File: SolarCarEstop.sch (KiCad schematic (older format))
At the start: 49 parts

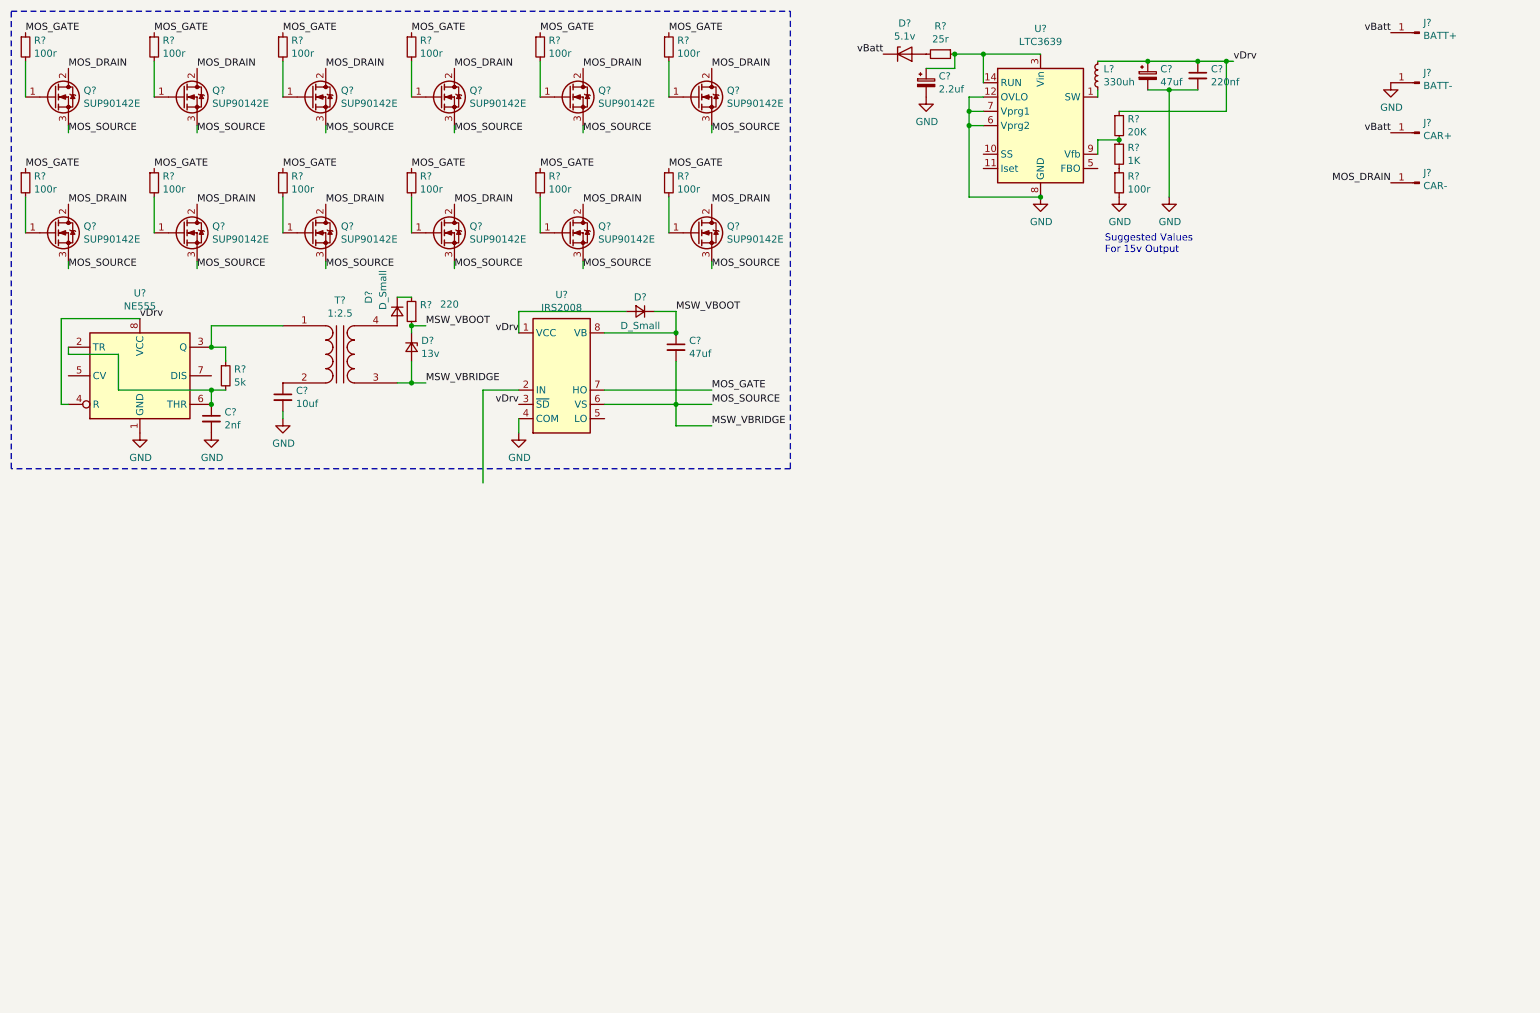
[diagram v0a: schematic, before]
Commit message: Add emergency button, BMS fault output, and BMS fault input
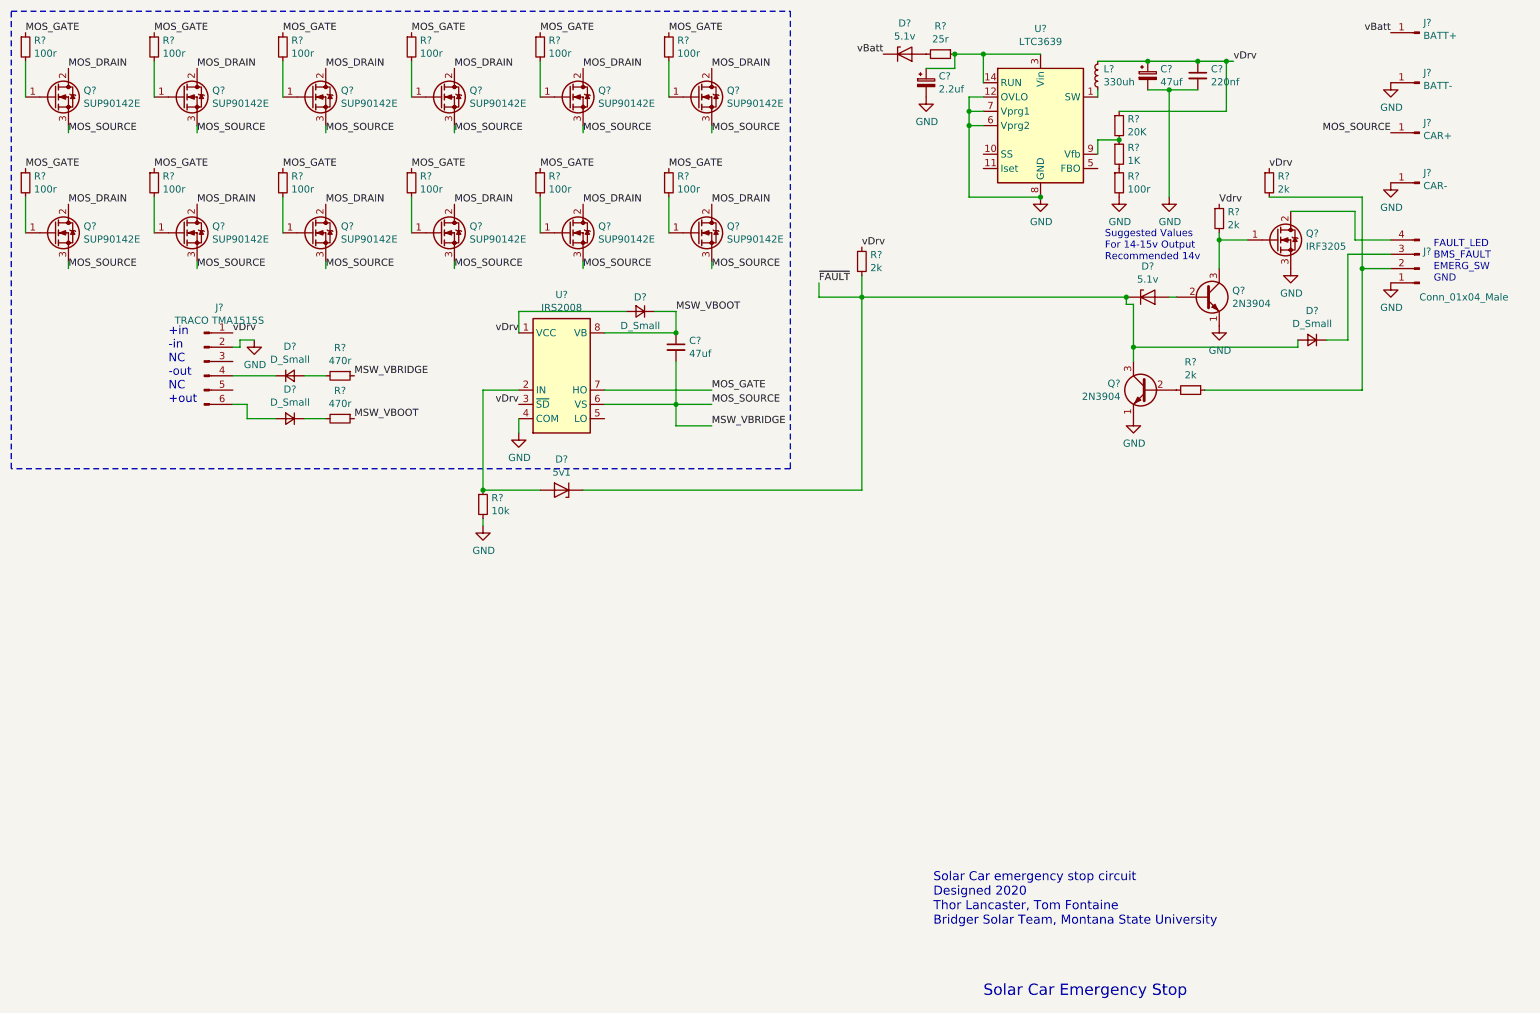
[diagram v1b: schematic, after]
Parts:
- removed C?: 10uf, symbol Device:C_Small
- removed C?: 2nf, symbol Device:C_Small
- removed D?: D_Small, symbol Device:D_Small
- removed D?: 13v, symbol Device:D_Zener_Small
- removed R?: 220, symbol Device:R_Small
- removed R?: 5k, symbol Device:R_Small
- removed T?: 1:2.5, symbol Device:Transformer_1P_1S
- removed U?: NE555, symbol Timer:NE555
- added D? (x3): D_Small, symbol Device:D_Small
- added D?: 5.1v, symbol Device:D_Zener
- added D?: 5v1, symbol Device:D_Zener
- added J?: TRACO TMA1515S, symbol Connector:Conn_01x06_Male
- added J?: Conn_01x04_Male, symbol Connector:Conn_01x04_Male
- added Q?: IRF3205, Package_TO_SOT_THT:TO-220-3_Vertical, symbol Transistor_FET:IRF3205
- added Q? (x2): 2N3904, Package_TO_SOT_THT:TO-92_Inline, symbol Transistor_BJT:2N3904
- added R? (x2): 470r, symbol Device:R_Small
- added R? (x4): 2k, symbol Device:R_Small
- added R?: 10k, symbol Device:R_Small
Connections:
- net GND: now also J?.1 (Pin_1), J?.1 (Pin_1), J?.2 (Pin_2), Q?.1 (E), Q?.1 (E), Q?.3 (S), R?.2
- net MOS_DRAIN: no longer J?.1 (Pin_1)
- net MOS_SOURCE: now also J?.1 (Pin_1), R?.1
- net MSW_VBOOT: now also R?.1
- net vBatt: no longer J?.1 (Pin_1)
- net vDrv: now also J?.1 (Pin_1), R?.1, R?.1
- net at U?.2 (IN): now also D?.2 (A), R?.1
- new net: D?.1 (K), J?.4 (Pin_4)
- new net: D?.2 (A), J?.6 (Pin_6)
- new net: D?.2 (A), R?.2
- new net: D?.1 (K), R?.2
- new net: J?.2 (Pin_2), R?.1, R?.2
- new net: D?.1 (K), J?.3 (Pin_3)
- new net: J?.4 (Pin_4), Q?.2 (D)
- new net: Q?.1 (G), Q?.3 (C), R?.2
- new net: D?.2 (A), Q?.2 (B)
- new net: Q?.2 (B), R?.2
- new net Vdrv: R?.1
- new net ~FAULT: D?.1 (K), D?.1 (K), D?.2 (A), Q?.3 (C), R?.2
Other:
- note added: "+in\n-in\nNC\n-out\nNC\n+out"
- note added: "FAULT_LED\nBMS_FAULT\nEMERG_SW\nGND"
- note added: "Solar Car Emergency Stop"
- note added: "Solar Car emergency stop circuit\nDesigned 2020\nThor Lancaster, Tom Fontaine\nBridger Solar Team, Montana State University"
- note added: "Suggested Values\nFor 14-15v Output\nRecommended 14v"
- note removed: "Suggested Values\nFor 15v Output"
